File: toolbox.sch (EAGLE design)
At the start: 81 parts, among them IC1 PIC18F4XK22PT, IC3 78L05SMD, T1 BC847, U2 AD654JRZ, U3 ADUM7441ARQZ

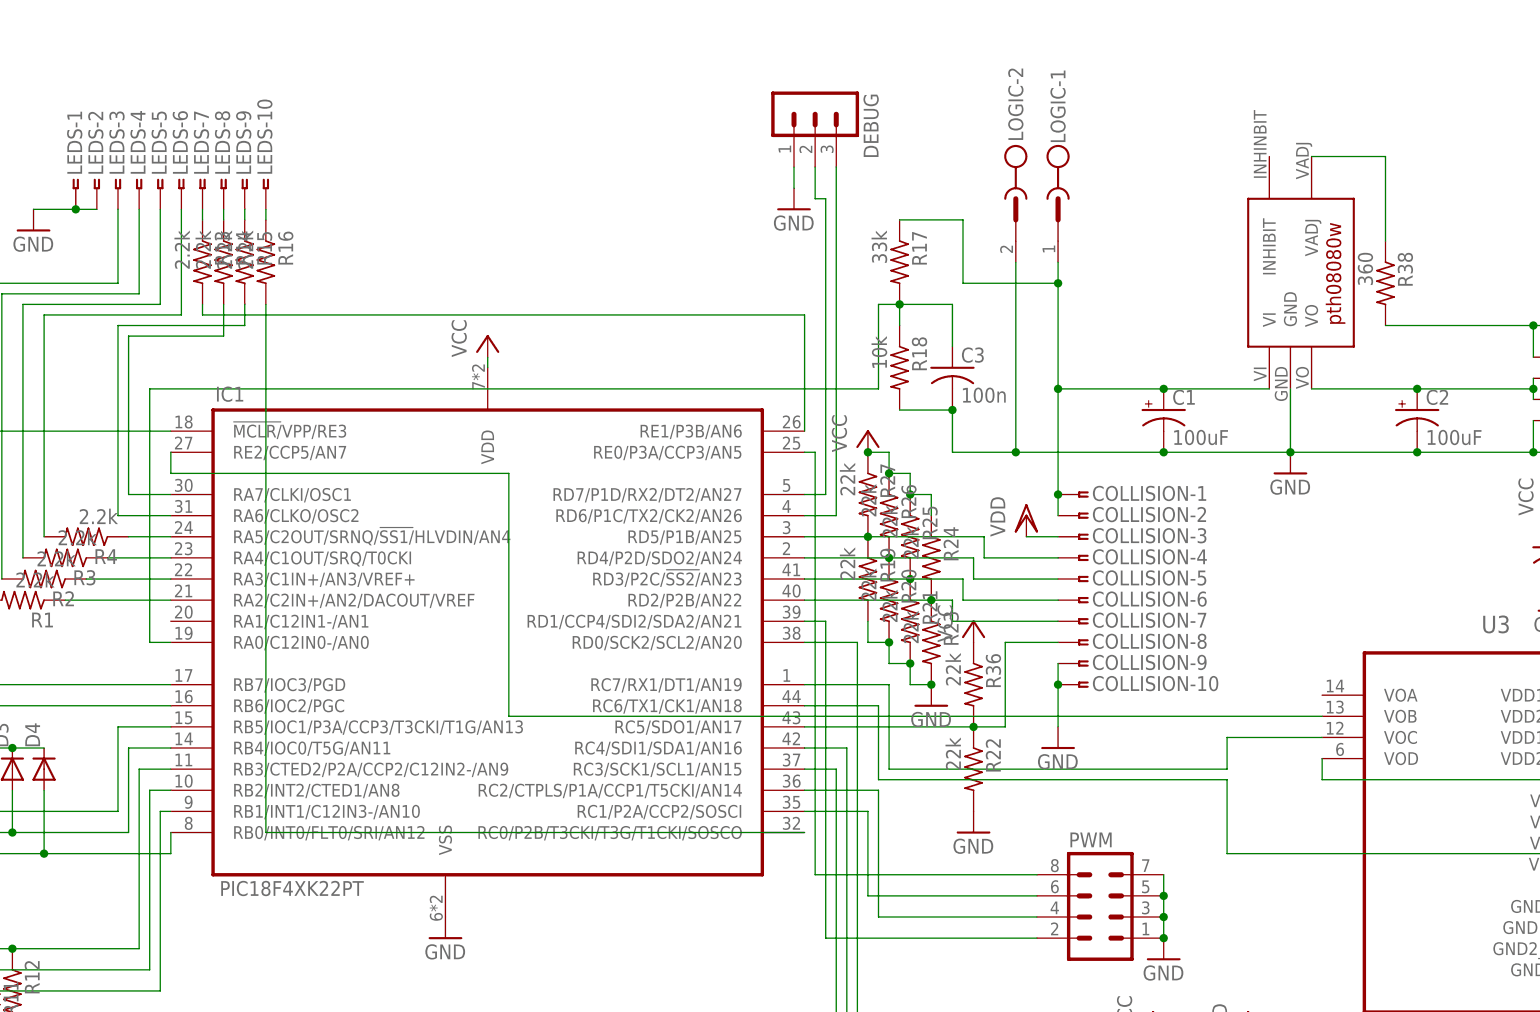
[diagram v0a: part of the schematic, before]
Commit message: added clipping circuit for collision sensors
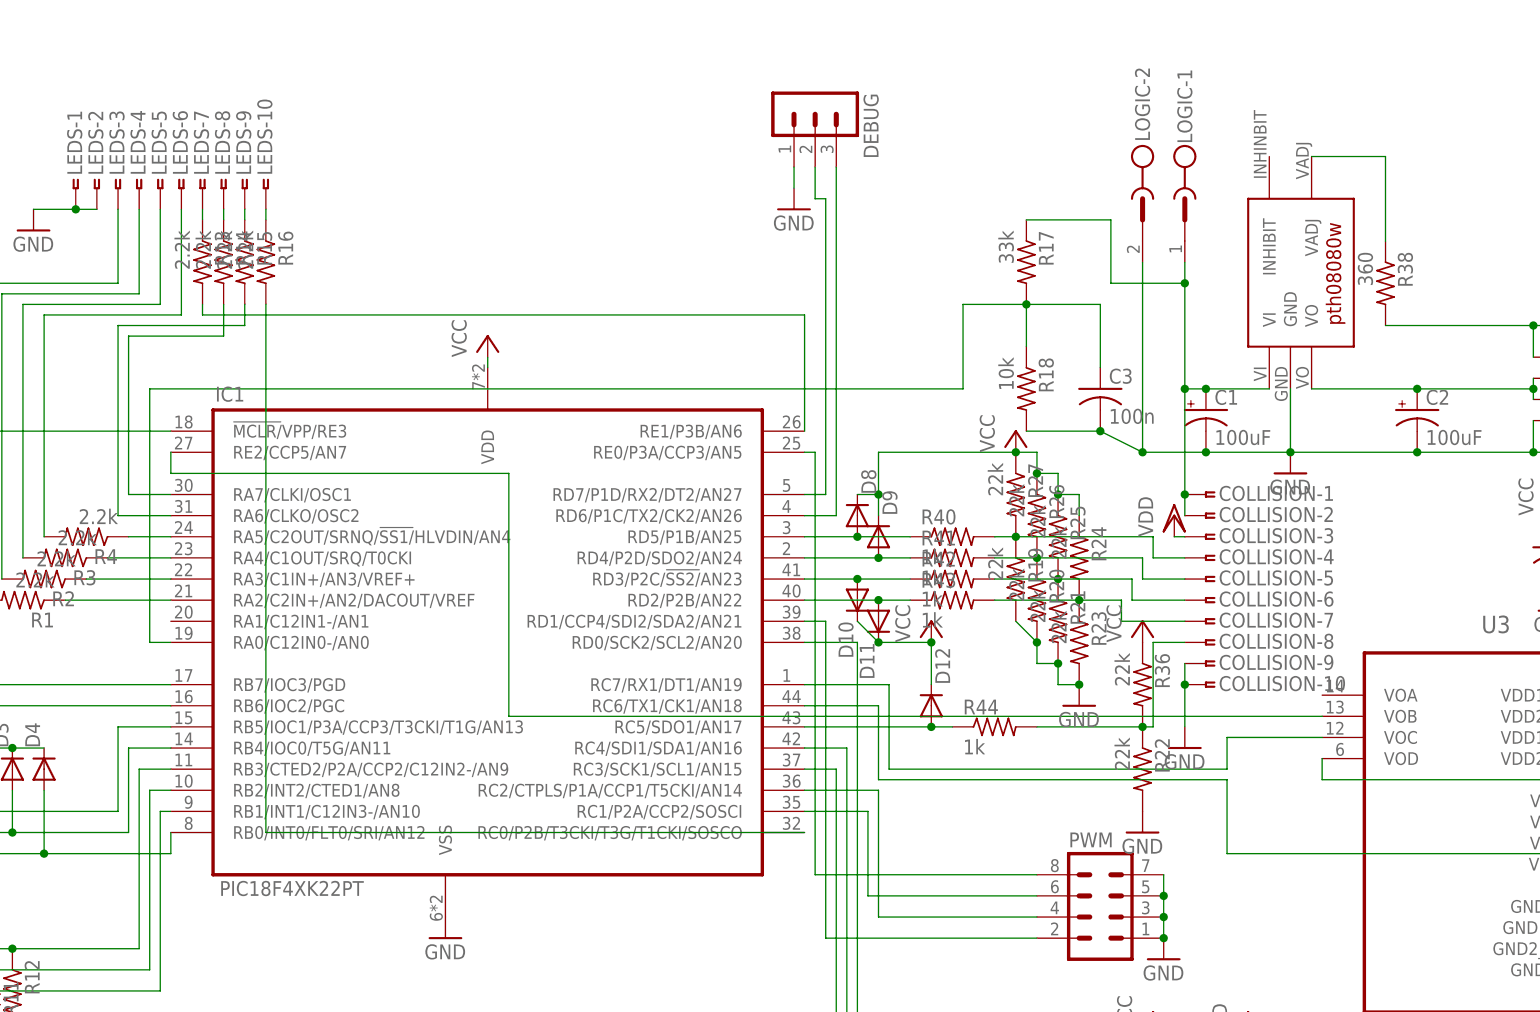
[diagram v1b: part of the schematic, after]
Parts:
- added D10, D11, D12, D8, D9: (no value), diode:DIODE-SOD523
- added R40, R41, R42, R43, R44: 1k, rcl:R-US_M0805
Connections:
- new net N$66: D12.A, IC1.RC5/SDO1/AN17, R44.1
- new net N$67: D8.A, IC1.RD5/P1B/AN25, R40.1
- new net N$69: D9.A, IC1.RD4/P2D/SDO2/AN24, R41.1
- new net N$70: D10.A, IC1.RD3/P2C/!SS2/!AN23, R42.1
- new net N$71: D11.A, IC1.RD2/P2B/AN22, R43.1
- net N$41: now also R40.2; no longer IC1.RD5/P1B/AN25
- net N$42: now also R41.2; no longer IC1.RD4/P2D/SDO2/AN24
- net N$43: now also R42.2; no longer IC1.RD3/P2C/!SS2/!AN23
- net N$44: now also R43.2; no longer IC1.RD2/P2B/AN22
- net N$45: now also R44.2; no longer IC1.RC5/SDO1/AN17
- net VCC: now also D10.C, D11.C, D12.C, D8.C, D9.C
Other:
- moved on the sheet: C1, C3, COLLISION-1, COLLISION-10, COLLISION-2, COLLISION-3, COLLISION-4, COLLISION-5, COLLISION-6, COLLISION-7, COLLISION-8, COLLISION-9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

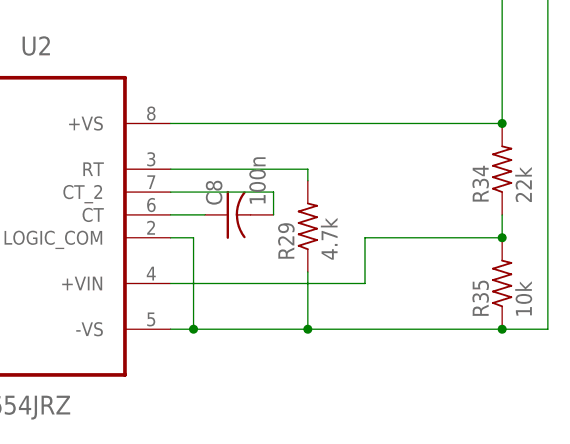
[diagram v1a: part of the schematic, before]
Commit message: circuit checked, added filtering capacitor and fixed a last clearance error
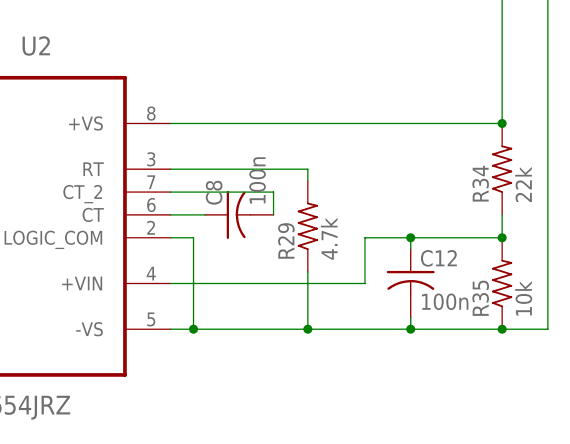
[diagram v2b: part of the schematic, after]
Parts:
- added C12: 100n, rcl:C-USC0805
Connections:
- net GND_MOTOR: now also C12.2
- net N$49: now also C12.1
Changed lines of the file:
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@@
 <part name="P+15" library="supply1" deviceset="VCC" device=""/>
 <part name="D12" library="diode" deviceset="DIODE-" device="SOD523"/>
+<part name="C12" library="rcl" deviceset="C-US" device="C0805" value="100n"/>
 </parts>
 <sheets>
@@
 <instance part="P+15" gate="VCC" x="116.84" y="48.26"/>
 <instance part="D12" gate="G$1" x="116.84" y="38.1" rot="MR90"/>
+<instance part="C12" gate="G$1" x="267.97" y="-24.13"/>
 </instances>
 <busses>
@@
 <pinref part="R35" gate="G$1" pin="2"/>
 <wire x1="278.13" y1="-17.78" x2="278.13" y2="-20.32" width="0.1524" layer="91"/>
-<wire x1="278.13" y1="-20.32" x2="262.89" y2="-20.32" width="0.1524" layer="91"/>
+<wire x1="278.13" y1="-20.32" x2="267.97" y2="-20.32" width="0.1524" layer="91"/>
 <junction x="278.13" y="-20.32"/>
 <pinref part="U2" gate="A" pin="+VIN"/>
+<wire x1="267.97" y1="-20.32" x2="262.89" y2="-20.32" width="0.1524" layer="91"/>
 <wire x1="262.89" y1="-20.32" x2="262.89" y2="-25.4" width="0.1524" layer="91"/>
 <wire x1="262.89" y1="-25.4" x2="241.3" y2="-25.4" width="0.1524" layer="91"/>
+<pinref part="C12" gate="G$1" pin="1"/>
+<wire x1="267.97" y1="-21.59" x2="267.97" y2="-20.32" width="0.1524" layer="91"/>
+<junction x="267.97" y="-20.32"/>
 </segment>
 </net>
@@
 <wire x1="283.21" y1="76.2" x2="242.57" y2="76.2" width="0.1524" layer="91"/>
 <junction x="242.57" y="76.2"/>
-<wire x1="256.54" y1="-30.48" x2="278.13" y2="-30.48" width="0.1524" layer="91"/>
+<wire x1="256.54" y1="-30.48" x2="267.97" y2="-30.48" width="0.1524" layer="91"/>
 <junction x="256.54" y="-30.48"/>
 <pinref part="R35" gate="G$1" pin="1"/>
+<wire x1="267.97" y1="-30.48" x2="278.13" y2="-30.48" width="0.1524" layer="91"/>
 <wire x1="278.13" y1="-30.48" x2="283.21" y2="-30.48" width="0.1524" layer="91"/>
 <junction x="278.13" y="-30.48"/>
@@
 <wire x1="209.55" y1="26.67" x2="209.55" y2="33.02" width="0.1524" layer="91"/>
 <junction x="209.55" y="26.67"/>
-</segment>
-</net>
+<pinref part="C12" gate="G$1" pin="2"/>
+<wire x1="267.97" y1="-29.21" x2="267.97" y2="-30.48" width="0.1524" layer="91"/>
+<junction x="267.97" y="-30.48"/>
+</segment>
+</net>
